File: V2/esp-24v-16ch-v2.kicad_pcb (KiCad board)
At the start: 2 copper layers, 138 x 67.8 mm, 268 parts, among them J1 VIN, J2 USB_C_Receptacle_USB2.0, J3 DB141V-2.54-8P, J4 DB141V-2.54-8P, J5 DB141V-2.54-8P, J6 DB141V-2.54-8P, J7 ETHERNET, Q1 WPM2015-3/TR, Q10 MMBT2222A/SOT-23-3, Q11 MMBT2222A/SOT-23-3, Q12 MMBT2222A/SOT-23-3, Q13 MMBT2222A/SOT-23-3, Q14 MMBT2222A/SOT-23-3, Q15 MMBT2222A/SOT-23-3, Q16 MMBT2222A/SOT-23-3, Q17 MMBT2222A/SOT-23-3, Q18 MMBT2222A/SOT-23-3, Q19 MMBT2222A/SOT-23-3, Q2 LMUN2211LT1G, Q3 UMH3N, Q4 MMBT2222A/SOT-23-3, Q5 MMBT2222A/SOT-23-3, Q6 MMBT2222A/SOT-23-3, Q7 MMBT2222A/SOT-23-3, Q8 MMBT2222A/SOT-23-3, Q9 MMBT2222A/SOT-23-3, SW1 RESET, U1 SY8089A1AAC, U10 OR-3H4-4, U11 OR-3H4-4, U2 TX4138, U3 CH340C, U4 ESP32-WROOM-32UE-N16, U5 LAN8710A, U6 MCP23017_SS, U7 MCP23017_SS, U8 OR-3H4-4, U9 OR-3H4-4

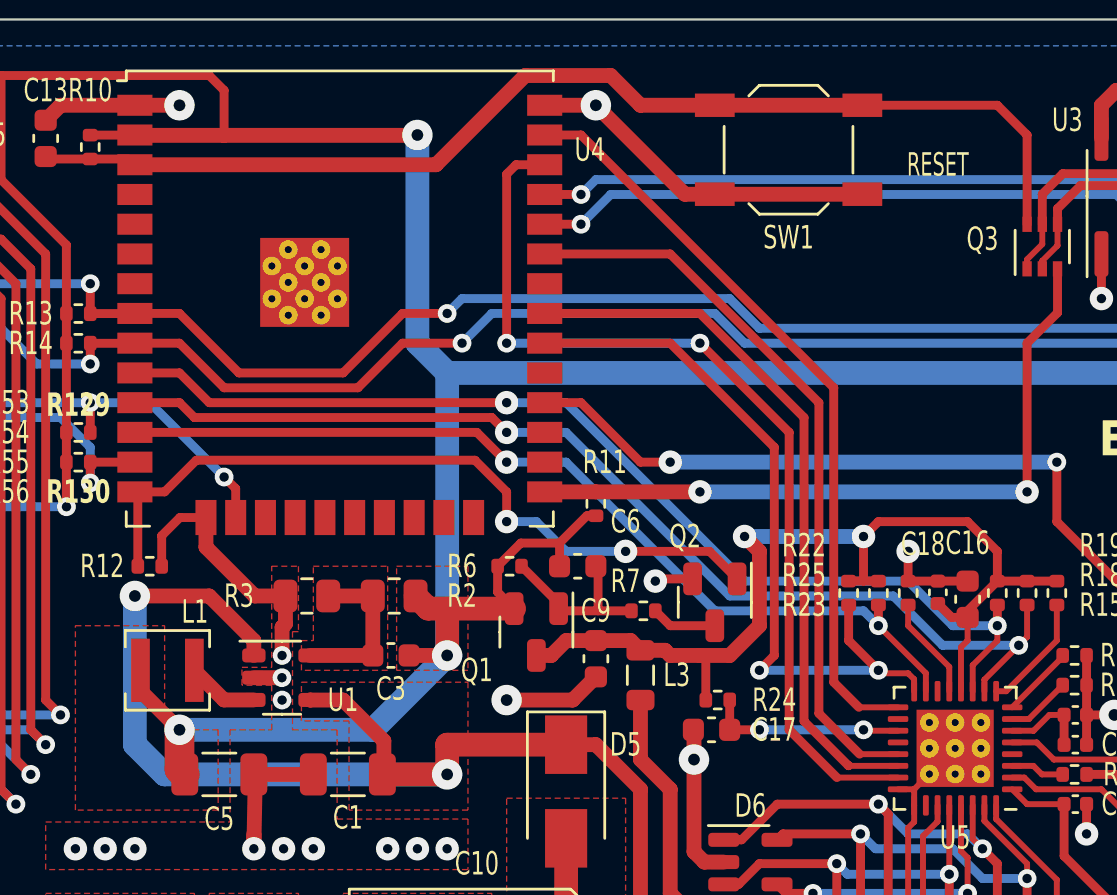
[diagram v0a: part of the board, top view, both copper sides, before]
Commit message: Adjusted footprint
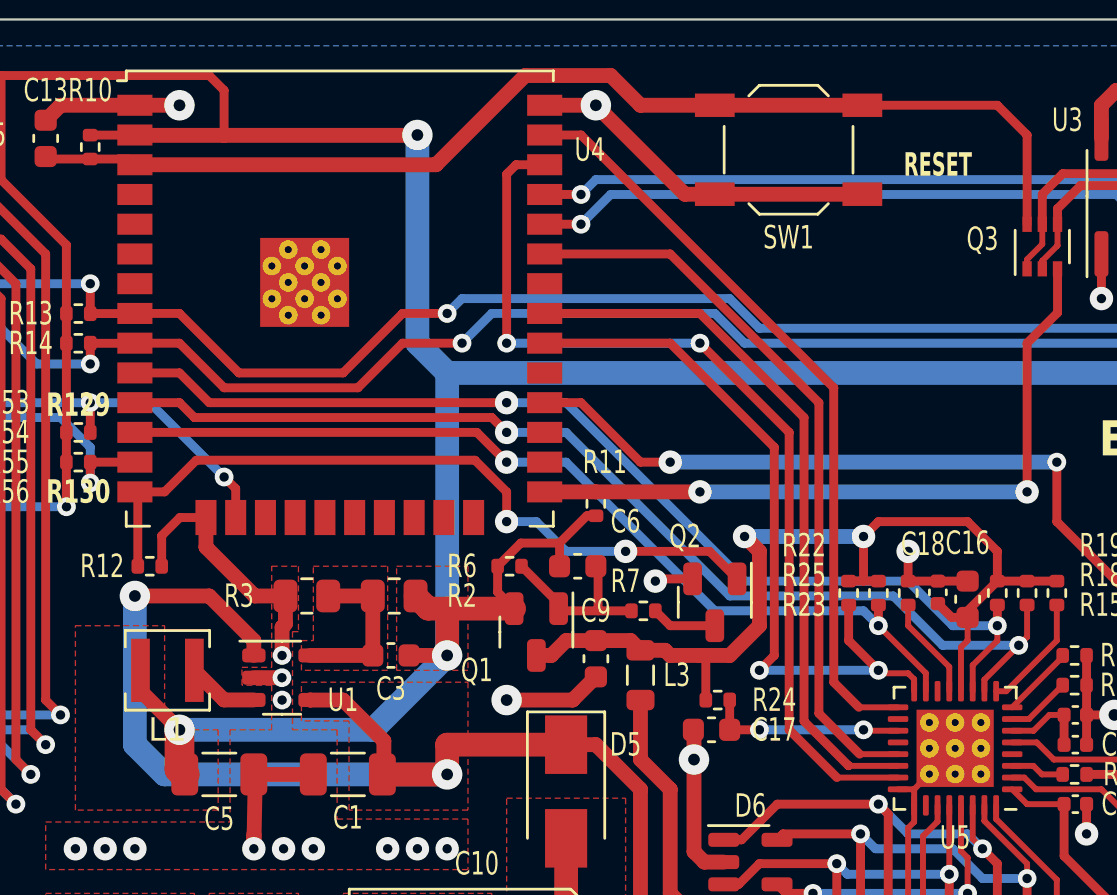
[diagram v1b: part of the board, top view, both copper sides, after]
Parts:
- L1: footprint Tales:L_3x3_h1.5 -> Tales:L_3x3mm_h1.5mm
